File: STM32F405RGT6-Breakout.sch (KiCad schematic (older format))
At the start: 30 parts

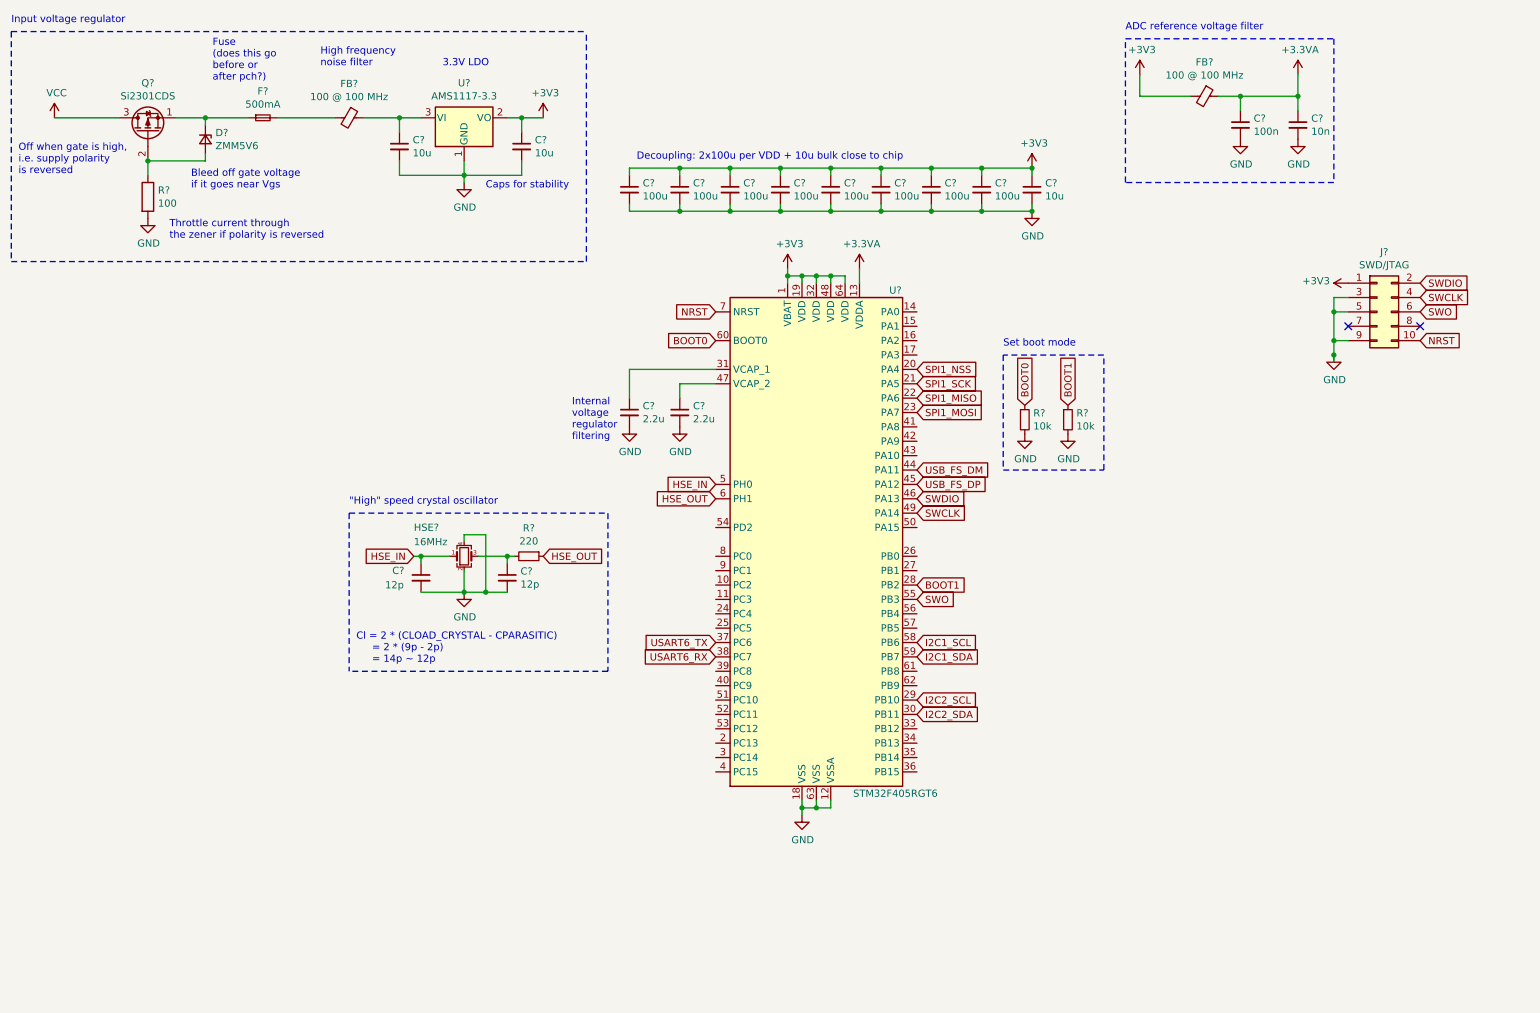
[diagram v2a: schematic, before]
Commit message: - i2c pullups - connectors laid out - added 3v3 and gnd to i2c connectors - working on adding USB
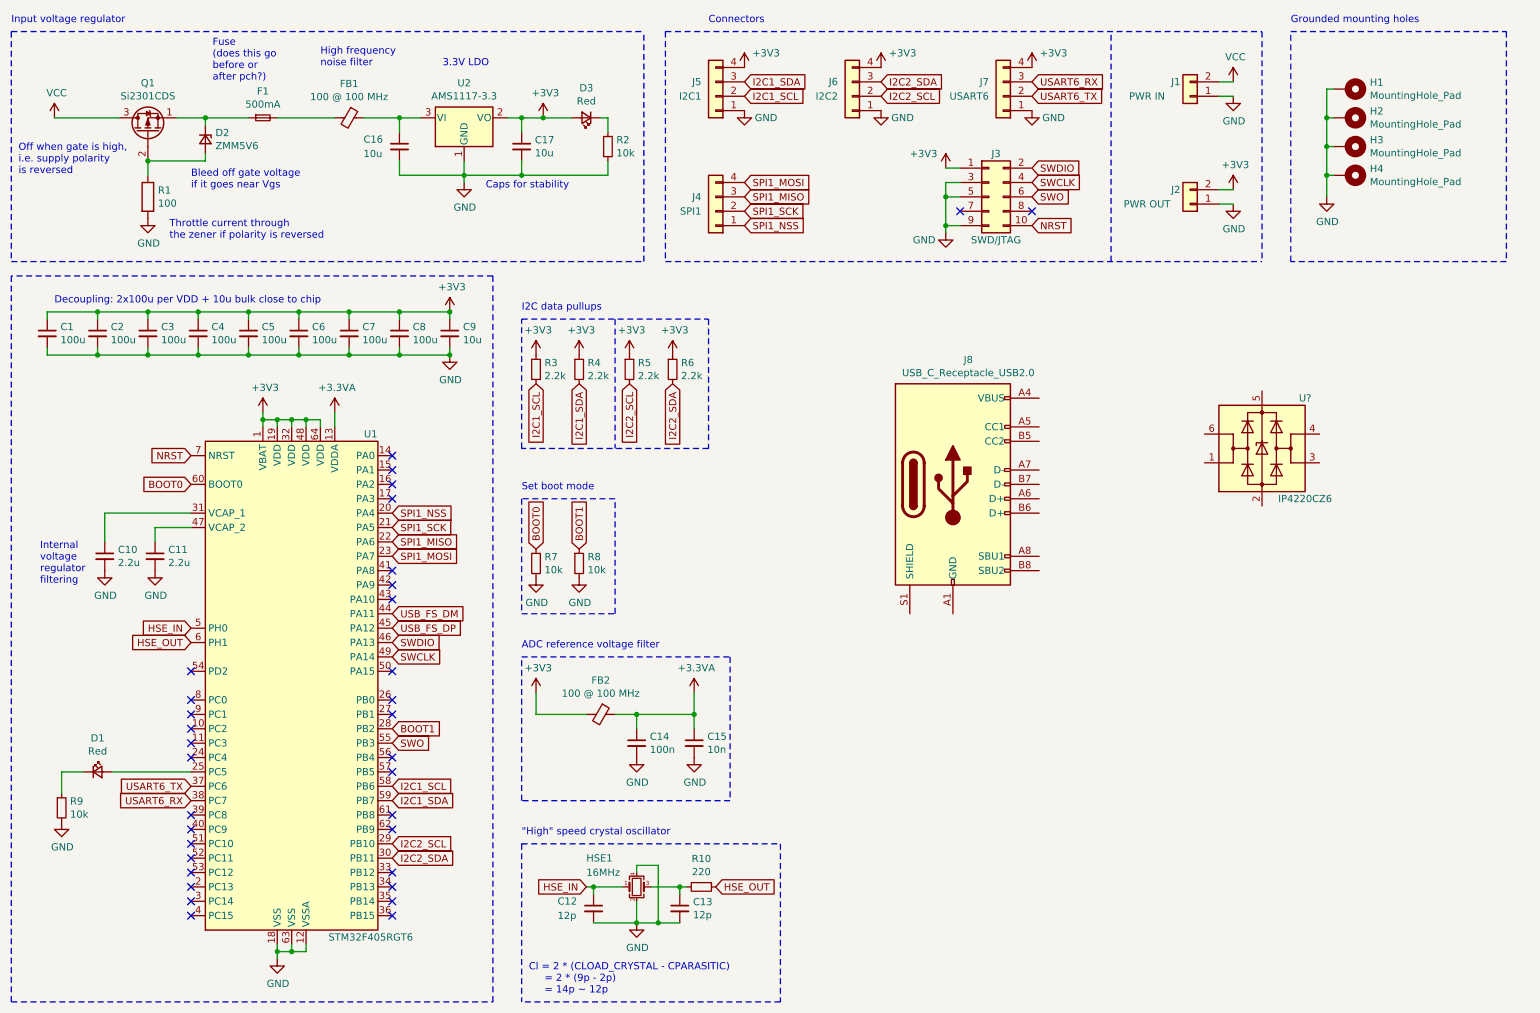
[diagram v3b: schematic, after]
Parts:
- added D1, D3: Red, symbol Device:LED_Small
- added H1, H2, H3, H4: MountingHole_Pad, symbol Mechanical:MountingHole_Pad
- added J1: PWR IN, symbol Connector_Generic:Conn_01x02
- added J2: PWR OUT, symbol Connector_Generic:Conn_01x02
- added J4: SPI1, symbol Connector_Generic:Conn_01x04
- added J5: I2C1, symbol Connector_Generic:Conn_01x04
- added J6: I2C2, symbol Connector_Generic:Conn_01x04
- added J7: USART6, symbol Connector_Generic:Conn_01x04
- added J8: USB_C_Receptacle_USB2.0, symbol Connector:USB_C_Receptacle_USB2.0
- added R2, R9: 10k, symbol Device:R_Small
- added R3, R4, R5, R6: 2.2k, symbol Device:R_Small
- added U?: IP4220CZ6, Package_TO_SOT_SMD:SOT-23-6, symbol Power_Protection:USBLC6-2SC6
- gave numbers to parts that had none: 30
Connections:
- net +3V3: now also D3.2 (A), J2.2 (Pin_2), J5.4 (Pin_4), J6.4 (Pin_4), J7.4 (Pin_4), R3.1, R4.1, R5.1, R6.1
- net GND: now also H1.1, H2.1, H3.1, H4.1, J1.1 (Pin_1), J2.1 (Pin_1), J5.1 (Pin_1), J6.1 (Pin_1), J7.1 (Pin_1), R2.2, R9.2
- net I2C1_SCL: now also J5.2 (Pin_2), R3.2
- net I2C1_SDA: now also J5.3 (Pin_3), R4.2
- net I2C2_SCL: now also J6.2 (Pin_2), R5.2
- net I2C2_SDA: now also J6.3 (Pin_3), R6.2
- net SPI1_MISO: now also J4.3 (Pin_3)
- net SPI1_MOSI: now also J4.4 (Pin_4)
- net SPI1_NSS: now also J4.1 (Pin_1)
- net SPI1_SCK: now also J4.2 (Pin_2)
- net USART6_RX: now also J7.3 (Pin_3)
- net USART6_TX: now also J7.2 (Pin_2)
- net VCC: now also J1.2 (Pin_2)
- net at U1.25 (PC5): now also D1.2 (A)
- new net: D1.1 (K), R9.1
- new net: D3.1 (K), R2.1
- new net: J8.A1 (GND), J8.A12 (GND), J8.B1 (GND), J8.B12 (GND)
- new net: J8.A4 (VBUS), J8.A9 (VBUS), J8.B4 (VBUS), J8.B9 (VBUS)
- no-connect marks 2 -> 34
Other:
- note added: "Connectors"
- note added: "Grounded mounting holes\n"
- note added: "I2C data pullups"
- moved on the sheet: C1, C10, C11, C12, C13, C14, C15, C2, C3, C4, C5, C6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

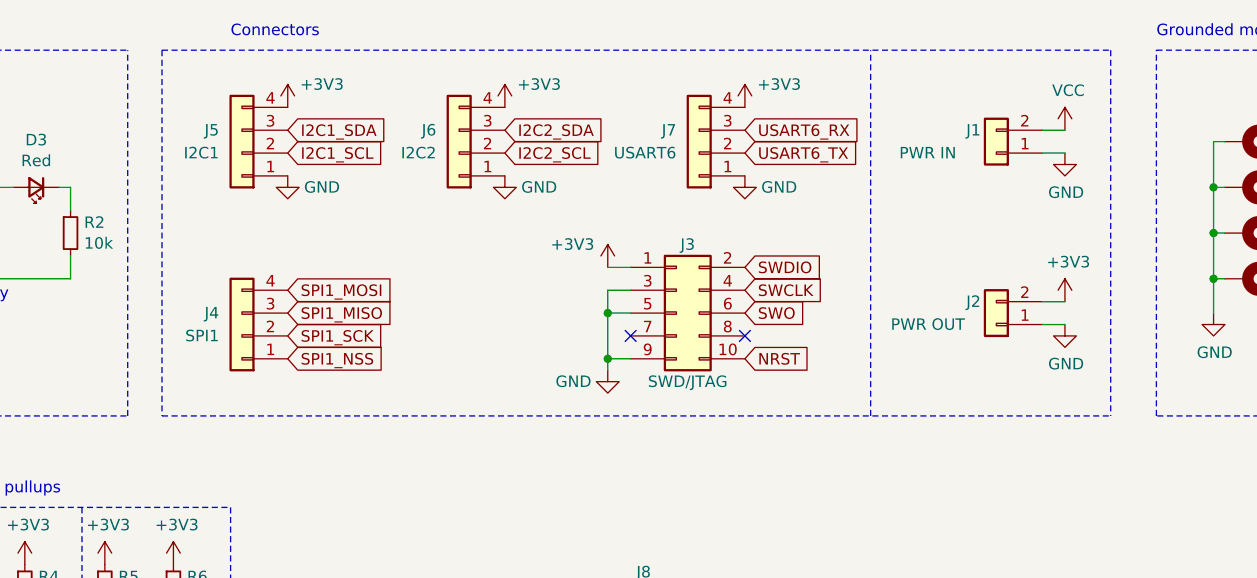
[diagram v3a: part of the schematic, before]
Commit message: get rid of Vin, we'll use USB only
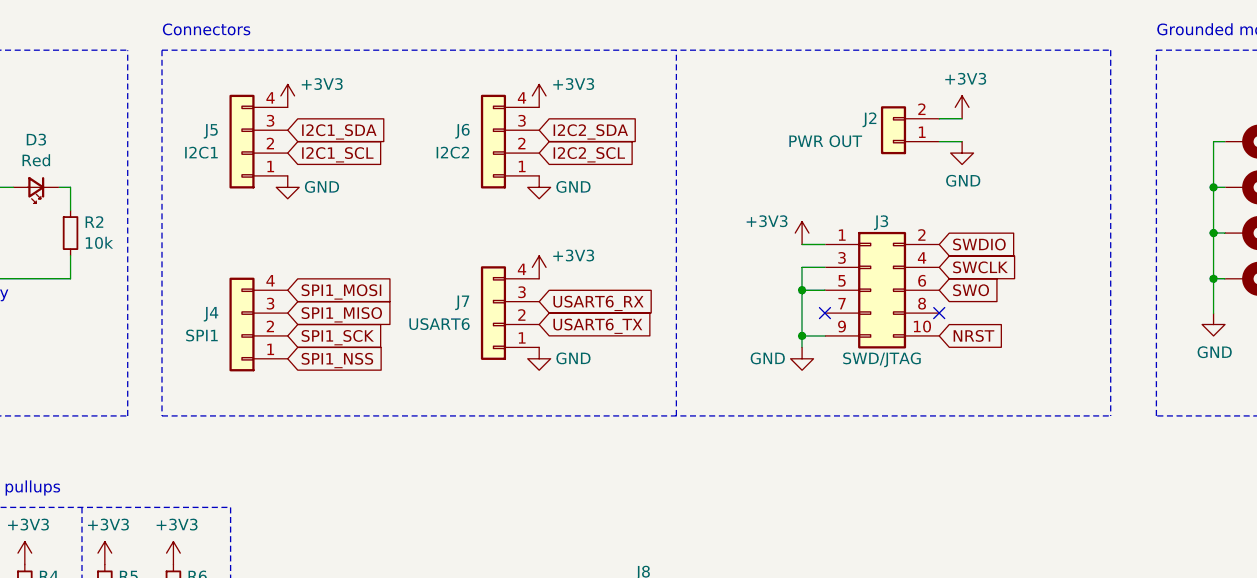
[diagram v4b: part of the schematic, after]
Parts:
- removed J1: PWR IN, symbol Connector_Generic:Conn_01x02
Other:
- moved on the sheet: J2, J3, J6, J7
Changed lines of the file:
@@
 L Connector_Generic:Conn_02x05_Odd_Even J3
 U 1 1 61A3C8B7
-P 7450 1900
-F 0 "J3" H 7500 2200 50  0000 C CNN
-F 1 "SWD/JTAG" H 7500 1600 50  0000 C CNN
-F 2 "" H 7450 1900 50  0001 C CNN
-F 3 "~" H 7450 1900 50  0001 C CNN
-	1    7450 1900
-	1    0    0    -1
-$EndComp
-NoConn ~ 7750 2000
-NoConn ~ 7250 2000
-Text GLabel 7750 1900 2    50   Input ~ 0
+P 8300 1800
+F 0 "J3" H 8350 2100 50  0000 C CNN
+F 1 "SWD/JTAG" H 8350 1500 50  0000 C CNN
+F 2 "" H 8300 1800 50  0001 C CNN
+F 3 "~" H 8300 1800 50  0001 C CNN
+	1    8300 1800
+	1    0    0    -1
+$EndComp
+NoConn ~ 8600 1900
+NoConn ~ 8100 1900
+Text GLabel 8600 1800 2    50   Input ~ 0
 SWO
-Text GLabel 7750 1700 2    50   Input ~ 0
+Text GLabel 8600 1600 2    50   Input ~ 0
 SWDIO
-Text GLabel 7750 1800 2    50   Input ~ 0
+Text GLabel 8600 1700 2    50   Input ~ 0
 SWCLK
 Wire Wire Line
-	7150 1800 7150 1900
-Wire Wire Line
-	7150 1800 7250 1800
-Wire Wire Line
-	7250 2100 7150 2100
-Connection ~ 7150 2100
-Wire Wire Line
-	7250 1900 7150 1900
-Connection ~ 7150 1900
-Wire Wire Line
-	7150 1900 7150 2100
-Text GLabel 7750 2100 2    50   Input ~ 0
+	8000 1700 8000 1800
+Wire Wire Line
+	8000 1700 8100 1700
+Wire Wire Line
+	8100 2000 8000 2000
+Connection ~ 8000 2000
+Wire Wire Line
+	8100 1800 8000 1800
+Connection ~ 8000 1800
+Wire Wire Line
+	8000 1800 8000 2000
+Text GLabel 8600 2000 2    50   Input ~ 0
 NRST
 Wire Wire Line
@@
 Text Notes 700  1750 0    50   ~ 0
 Off when gate is high,\ni.e. supply polarity \nis reversed
-Text GLabel 7750 1200 2    50   Input ~ 0
+Text GLabel 6850 1950 2    50   Input ~ 0
 USART6_TX
 Text GLabel 5750 1200 2    50   Input ~ 0
@@
 SPI1_MOSI
 Wire Notes Line
-	8300 2350 8300 750
+	7450 2350 7450 750
 Wire Notes Line
 	5200 750  5200 2350
-Text Notes 5500 700  0    50   ~ 0
+Text Notes 5200 700  0    50   ~ 0
 Connectors
 Wire Wire Line
@@
 	1    0    0    -1
 $EndComp
-Text GLabel 6700 1200 2    50   Input ~ 0
+Text GLabel 6850 1200 2    50   Input ~ 0
 I2C2_SCL
-Text GLabel 6700 1100 2    50   Input ~ 0
+Text GLabel 6850 1100 2    50   Input ~ 0
 I2C2_SDA
 $Comp
@@
 L Connector_Generic:Conn_01x04 J6
 U 1 1 61DC0149
-P 6500 1200
-F 0 "J6" H 6600 1100 50  0000 L CNN
-F 1 "I2C2" H 6600 1200 50  0000 L CNN
-F 2 "" H 6500 1200 50  0001 C CNN
-F 3 "~" H 6500 1200 50  0001 C CNN
-	1    6500 1200
+P 6650 1200
+F 0 "J6" H 6750 1100 50  0000 L CNN
+F 1 "I2C2" H 6750 1200 50  0000 L CNN
+F 2 "" H 6650 1200 50  0001 C CNN
+F 3 "~" H 6650 1200 50  0001 C CNN
+	1    6650 1200
 	-1   0    0    1
 $EndComp
@@
 L Connector_Generic:Conn_01x04 J7
 U 1 1 61DD83D6
-P 7550 1200
-F 0 "J7" H 7650 1100 50  0000 L CNN
-F 1 "USART6" H 7650 1200 50  0000 L CNN
-F 2 "" H 7550 1200 50  0001 C CNN
-F 3 "~" H 7550 1200 50  0001 C CNN
-	1    7550 1200
+P 6650 1950
+F 0 "J7" H 6750 1850 50  0000 L CNN
+F 1 "USART6" H 6750 1950 50  0000 L CNN
+F 2 "" H 6650 1950 50  0001 C CNN
+F 3 "~" H 6650 1950 50  0001 C CNN
+	1    6650 1950
 	-1   0    0    1
 $EndComp
-Text GLabel 7750 1100 2    50   Input ~ 0
+Text GLabel 6850 1850 2    50   Input ~ 0
 USART6_RX
 $Comp
 L power:+3V3 #PWR028
 U 1 1 61D29C38
-P 9150 1850
-F 0 "#PWR028" H 9150 1700 50  0001 C CNN
-F 1 "+3V3" H 9165 2023 50  0000 C CNN
-F 2 "" H 9150 1850 50  0001 C CNN
-F 3 "" H 9150 1850 50  0001 C CNN
-	1    9150 1850
+P 8700 1050
+F 0 "#PWR028" H 8700 900 50  0001 C CNN
+F 1 "+3V3" H 8715 1223 50  0000 C CNN
+F 2 "" H 8700 1050 50  0001 C CNN
+F 3 "" H 8700 1050 50  0001 C CNN
+	1    8700 1050
 	1    0    0    -1
 $EndComp
@@
 L Connector_Generic:Conn_01x02 J2
 U 1 1 61D2526B
-P 8850 1950
-F 0 "J2" H 8950 1850 50  0000 C CNN
-F 1 "PWR OUT" H 9150 1950 50  0000 C CNN
-F 2 "" H 8850 1950 50  0001 C CNN
-F 3 "~" H 8850 1950 50  0001 C CNN
-	1    8850 1950
+P 8400 1150
+F 0 "J2" H 8500 1050 50  0000 C CNN
+F 1 "PWR OUT" H 8700 1150 50  0000 C CNN
+F 2 "" H 8400 1150 50  0001 C CNN
+F 3 "~" H 8400 1150 50  0001 C CNN
+	1    8400 1150
 	-1   0    0    1
 $EndComp
 Wire Wire Line
-	9050 1850 9150 1850
-Wire Wire Line
-	9050 1950 9150 1950
+	8600 1050 8700 1050
+Wire Wire Line
+	8600 1150 8700 1150
 $Comp
 L power:GND #PWR029
 U 1 1 61D25255
-P 9150 1950
-F 0 "#PWR029" H 9150 1700 50  0001 C CNN
-F 1 "GND" H 9155 1777 50  0000 C CNN
-F 2 "" H 9150 1950 50  0001 C CNN
-F 3 "" H 9150 1950 50  0001 C CNN
-	1    9150 1950
-	1    0    0    -1
-$EndComp
-$Comp
-L Connector_Generic:Conn_01x02 J1
-U 1 1 61CF7673
-P 8850 1200
-F 0 "J1" H 8950 1100 50  0000 C CNN
-F 1 "PWR IN" H 9150 1200 50  0000 C CNN
-F 2 "" H 8850 1200 50  0001 C CNN
-F 3 "~" H 8850 1200 50  0001 C CNN
-	1    8850 1200
-	-1   0    0    1
-$EndComp
-Wire Wire Line
-	9050 1100 9150 1100
-$Comp
-L power:VCC #PWR026
-U 1 1 61CFCE24
-P 9150 1100
-F 0 "#PWR026" H 9150 950 50  0001 C CNN
-F 1 "VCC" H 9165 1273 50  0000 C CNN
-F 2 "" H 9150 1100 50  0001 C CNN
-F 3 "" H 9150 1100 50  0001 C CNN
-	1    9150 1100
-	1    0    0    -1
-$EndComp
-Wire Wire Line
-	9050 1200 9150 1200
-$Comp
-L power:GND #PWR027
-U 1 1 61CF863F
-P 9150 1200
-F 0 "#PWR027" H 9150 950 50  0001 C CNN
-F 1 "GND" H 9155 1027 50  0000 C CNN
-F 2 "" H 9150 1200 50  0001 C CNN
-F 3 "" H 9150 1200 50  0001 C CNN
-	1    9150 1200
-	1    0    0    -1
-$EndComp
-Wire Wire Line
-	7150 2100 7150 2150
+P 8700 1150
+F 0 "#PWR029" H 8700 900 50  0001 C CNN
+F 1 "GND" H 8705 977 50  0000 C CNN
+F 2 "" H 8700 1150 50  0001 C CNN
+F 3 "" H 8700 1150 50  0001 C CNN
+	1    8700 1150
+	1    0    0    -1
+$EndComp
+Wire Wire Line
+	8000 2000 8000 2050
 $Comp
 L power:GND #PWR024
 U 1 1 61A43965
-P 7150 2150
-F 0 "#PWR024" H 7150 1900 50  0001 C CNN
-F 1 "GND" H 7000 2100 50  0000 C CNN
-F 2 "" H 7150 2150 50  0001 C CNN
-F 3 "" H 7150 2150 50  0001 C CNN
-	1    7150 2150
+P 8000 2050
+F 0 "#PWR024" H 8000 1800 50  0001 C CNN
+F 1 "GND" H 7850 2000 50  0000 C CNN
+F 2 "" H 8000 2050 50  0001 C CNN
+F 3 "" H 8000 2050 50  0001 C CNN
+	1    8000 2050
 	1    0    0    -1
 $EndComp
@@
 L power:+3V3 #PWR?
 U 1 1 61E54E72
-P 6700 1000
-F 0 "#PWR?" H 6700 850 50  0001 C CNN
-F 1 "+3V3" H 6850 1100 50  0000 C CNN
-F 2 "" H 6700 1000 50  0001 C CNN
-F 3 "" H 6700 1000 50  0001 C CNN
-	1    6700 1000
+P 6850 1000
+F 0 "#PWR?" H 6850 850 50  0001 C CNN
+F 1 "+3V3" H 7000 1100 50  0000 C CNN
+F 2 "" H 6850 1000 50  0001 C CNN
+F 3 "" H 6850 1000 50  0001 C CNN
+	1    6850 1000
 	1    0    0    -1
 $EndComp
@@
 L power:+3V3 #PWR?
 U 1 1 61E55F38
-P 7750 1000
-F 0 "#PWR?" H 7750 850 50  0001 C CNN
-F 1 "+3V3" H 7900 1100 50  0000 C CNN
-F 2 "" H 7750 1000 50  0001 C CNN
-F 3 "" H 7750 1000 50  0001 C CNN
-	1    7750 1000
+P 6850 1750
+F 0 "#PWR?" H 6850 1600 50  0001 C CNN
+F 1 "+3V3" H 7000 1850 50  0000 C CNN
+F 2 "" H 6850 1750 50  0001 C CNN
+F 3 "" H 6850 1750 50  0001 C CNN
+	1    6850 1750
 	1    0    0    -1
 $EndComp
@@
 L power:GND #PWR?
 U 1 1 61E565AA
-P 7750 1300
-F 0 "#PWR?" H 7750 1050 50  0001 C CNN
-F 1 "GND" H 7900 1250 50  0000 C CNN
-F 2 "" H 7750 1300 50  0001 C CNN
-F 3 "" H 7750 1300 50  0001 C CNN
-	1    7750 1300
+P 6850 2050
+F 0 "#PWR?" H 6850 1800 50  0001 C CNN
+F 1 "GND" H 7000 2000 50  0000 C CNN
+F 2 "" H 6850 2050 50  0001 C CNN
+F 3 "" H 6850 2050 50  0001 C CNN
+	1    6850 2050
 	1    0    0    -1
 $EndComp
@@
 L power:GND #PWR?
 U 1 1 61E55AA2
-P 6700 1300
-F 0 "#PWR?" H 6700 1050 50  0001 C CNN
-F 1 "GND" H 6850 1250 50  0000 C CNN
-F 2 "" H 6700 1300 50  0001 C CNN
-F 3 "" H 6700 1300 50  0001 C CNN
-	1    6700 1300
+P 6850 1300
+F 0 "#PWR?" H 6850 1050 50  0001 C CNN
+F 1 "GND" H 7000 1250 50  0000 C CNN
+F 2 "" H 6850 1300 50  0001 C CNN
+F 3 "" H 6850 1300 50  0001 C CNN
+	1    6850 1300
 	1    0    0    -1
 $EndComp
@@
 $EndComp
 Wire Wire Line
-	7250 1700 7150 1700
+	8100 1600 8000 1600
 $Comp
 L power:+3V3 #PWR025
 U 1 1 61A41135
-P 7150 1700
-F 0 "#PWR025" H 7150 1550 50  0001 C CNN
-F 1 "+3V3" H 6900 1800 50  0000 L CNN
-F 2 "" H 7150 1700 50  0001 C CNN
-F 3 "" H 7150 1700 50  0001 C CNN
-	1    7150 1700
-	1    0    0    -1
-$EndComp
+P 8000 1600
+F 0 "#PWR025" H 8000 1450 50  0001 C CNN
+F 1 "+3V3" H 7750 1700 50  0000 L CNN
+F 2 "" H 8000 1600 50  0001 C CNN
+F 3 "" H 8000 1600 50  0001 C CNN
+	1    8000 1600
+	1    0    0    -1
+$EndComp

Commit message: - USB-C connector wired in with ESD protection. - We can't get the USBLC6-2SC6 chip except in full reels, so sub in the IP4220CZ6 (https://datasheet.lcsc.com/lcsc/1810121050_Nexperia-IP4220CZ6,125_C282546.pdf) and hope it works
- Still looking for a USB connector that's available in 1+ qty and has a footprint we can get
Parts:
- added R11, R12: 5.1k, symbol Device:R_Small
- FB2: value 100 @ 100 MHz -> 100 @ 100 MHz
- gave numbers to parts that had none: 1
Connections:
- net USB_FS_DM is gone; now on net USB_D-: U1.44 (PA11)
- net USB_FS_DP is gone; now on net USB_D+: U1.45 (PA12)
- net VCC is gone; now on net +5V: Q1.3 (D)
- net GND: now also J8.A1 (GND), J8.A12 (GND), J8.B1 (GND), J8.B12 (GND), U3.2 (GND), R11.1, R12.1
- net +5V: now reaches J8.A4 (VBUS), J8.A9 (VBUS), J8.B4 (VBUS), J8.B9 (VBUS)
- net +5V: now also U3.5 (VBUS)
- net at J8.A5 (CC1): now also R11.2
- net USB_CONN_D+: now reaches J8.A6 (D+)
- net USB_CONN_D+: now also J8.B6 (D+), U3.3 (I/O2)
- net USB_CONN_D-: now reaches J8.A7 (D-)
- net USB_CONN_D-: now also J8.B7 (D-), U3.1 (I/O1)
- net at J8.B5 (CC2): now also R12.2
- net USB_D+: now reaches U3.4 (I/O2)
- net USB_D-: now reaches U3.6 (I/O1)
- no-connect marks 34 -> 37
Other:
- note added: ""Supporting Type-C from an existing USB2.0 design is straightforward and cheap \n(except for the connector). Basically you tie the DP pins together, tie the DM pins \ntogether, and add one pull-down resistor to each CC pin. This new Type-C device \nwill identify as a data and power sink, use the default USB2.0 power of 500 mA, \nand work in either orientation of the plug.""
- note added: "Main power rail"
- note added: "Power indicator\n\n"
- note added: "Push spikes >5V up the ladder \nand shunt down to ground.\n(at least I think that's how it works)"
- note added: "The shield is\ngrounded at \nthe host."
- note added: "USB in\n\n"
- note added: "USB-C (USB2.0)"
- note added: "USB2.0 cables don't\nconnect to SBU, so \nwe can leave it floating."
- moved on the sheet: C14, C15, FB2, J8, R3, R4, R5, R6, U3
